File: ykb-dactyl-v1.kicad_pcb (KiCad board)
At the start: 2 copper layers, 55.7 x 57.2 mm, 68 parts, among them IC1 TXU0101DCKR, J1 JST_SH_BM10B-SRSS-TB_1x10-1MP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, J10 Conn_01x05, J11 Conn_01x02_MountingPin, J2 JST_SH_BM10B-SRSS-TB_1x10-1MP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, J3 JST_SH_BM10B-SRSS-TB_1x10-1MP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, J4 JST_SH_BM10B-SRSS-TB_1x10-1MP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, J5 JST_SH_BM10B-SRSS-TB_1x10-1MP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, J6 JST_SH_BM10B-SRSS-TB_1x10-1MP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, J7 JST_SH_BM12B-SRSS-TB_1x12-1MP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

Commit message: Add first version to the silkscreen
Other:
- board text added: "DV1_MB_REV_1.0"
- board text added: "Developer Preview 1"
- board text added: "YarmanKB"

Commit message: Update
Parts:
- added R7: 100K, Resistor_SMD:R_0402_1005Metric, F.Cu at (186.2, 112.8)
- added R8: 200K, Resistor_SMD:R_0402_1005Metric, F.Cu at (185.0, 112.8)
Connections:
- U1 pad P1.3: unconnected-(U1B-P1.03-PadP1.3) -> CHARGER_EN
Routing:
- net CHARGER_EN: track 0.00 -> 19.8 mm, vias 0 -> 2
- net +5V_USB: track 50.3 -> 62.3 mm, vias 2 -> 4
- net BAT_STAT_1: track 75.5 -> 78.0 mm
- net MUX3_A2: track 46.5 -> 48.5 mm
- net GND: track 39.6 -> 41.0 mm, vias 21 -> 42
- net MUX3_A1: track 47.5 -> 48.7 mm
- net MUX4_D: track 58.7 -> 59.7 mm
- net MUX3_A0: track 42.5 -> 43.4 mm
- net /MCU/RESET: track 57.8 -> 58.6 mm
- net /MCU/DBG_UART_NETCORE_RX: track 38.4 -> 39.0 mm

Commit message: Developer Preview 1
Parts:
- moved R4 0.90 mm to (175.0, 67.8)
- moved R5 0.90 mm to (175.0, 69.0)
- moved R6 0.90 mm to (175.0, 66.6)
- moved R71 0.20 mm to (179.5, 105.3)
- moved R72 0.20 mm to (179.5, 106.4)
- moved R73 0.20 mm to (179.5, 104.2)
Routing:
- net /MUXes/MUX1_S2: track 16.9 -> 22.1 mm
- net /MUXes/MUX1_S3: track 18.0 -> 22.8 mm
- net USB_DN_P: track 45.5 -> 41.5 mm
- net /MUXes/MUX2_S6: track 15.5 -> 19.4 mm
- net /MUXes/MUX2_S7: track 17.4 -> 21.3 mm
- net MUX1_D: track 36.2 -> 40.1 mm
- net ALARMB: track 7.70 -> 11.6 mm
- net /MUXes/MUX1_S5: track 17.2 -> 20.9 mm
- net /MUXes/MUX4_S3: track 20.5 -> 24.1 mm
- net /MUXes/MUX1_S6: track 16.2 -> 19.7 mm
- net /MUXes/MUX4_S5: track 15.2 -> 18.7 mm
- net /MUXes/MUX3_S1: track 14.6 -> 18.0 mm
- net MUX4_D: track 59.7 -> 63.0 mm
- net SW_P: track 55.2 -> 51.9 mm
- net /MUXes/MUX1_S8: track 15.9 -> 19.2 mm
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
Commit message: Developer Preview 2
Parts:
- removed D3: RB751S40,115, footprints:RB751S40115
- removed R4, R5, R6: 10K, Resistor_SMD:R_0402_1005Metric
- removed R7: 100K, Resistor_SMD:R_0402_1005Metric
- removed R8: 200K, Resistor_SMD:R_0402_1005Metric
- added Q21: BC847W, Package_TO_SOT_SMD:SOT-323_SC-70, F.Cu at (192.4, 76.1)
- added Q91: BC847BDW1, Package_TO_SOT_SMD:SOT-363_SC-70-6, F.Cu at (172.3, 73.3)
- added Q92: BC847W, Package_TO_SOT_SMD:SOT-323_SC-70, F.Cu at (186.2, 112.4)
- added R24: 100K, Resistor_SMD:R_0402_1005Metric, F.Cu at (189.8, 73.9)
- added R91: 100K, Resistor_SMD:R_0402_1005Metric, F.Cu at (188.2, 110.7)
- added R92: 47K, Resistor_SMD:R_0402_1005Metric, F.Cu at (178.0, 111.2)
- added R93: 100K, Resistor_SMD:R_0402_1005Metric, F.Cu at (174.9, 67.8)
- added R94: 47K, Resistor_SMD:R_0402_1005Metric, F.Cu at (174.3, 75.5)
- added R95: 100K, Resistor_SMD:R_0402_1005Metric, F.Cu at (174.9, 69.0)
- added R96: 47K, Resistor_SMD:R_0402_1005Metric, F.Cu at (172.9, 76.3)
- C52: value 1uF -> 22uF
- L31: footprint Inductor_SMD:L_0402_1005Metric -> Inductor_SMD:L_1008_2520Metric
- L41: footprint Inductor_SMD:L_0402_1005Metric -> Inductor_SMD:L_Murata_DFE201610P
- R51: value 1K -> 620
- R52: value 5K -> 18K
- R97: renamed from R1; value 600 -> 10K
- R98: renamed from R2; value 600 -> 10K
- R99: renamed from R3; value 600 -> 5K
- U2: footprint footprints:SON40P150X150X50-9N -> footprints:USP-8B06
- U7: value LC709203FXE-03MH -> MAX17048G+T10; footprint footprints:WLCSP9_1P60X1P76_ONS -> footprints:21-0168E_T822-3_MXM
- moved R73 3.18 mm to (182.6, 103.5), turned to -90 degrees
- moved R72 2.57 mm to (178.9, 103.9)
- moved C42 1.70 mm to (198.6, 109.7)
- moved R71 1.12 mm to (179.0, 106.3)
- moved C71 1.04 mm to (180.3, 108.8)
- moved U7 0.93 mm to (182.2, 106.2), turned to 90 degrees
- moved L41 0.92 mm to (196.7, 109.9)
- moved R23 0.91 mm to (190.9, 73.9)
- moved L31 0.74 mm to (192.5, 104.3)
- moved R43 0.40 mm to (199.3, 112.1)
- moved R44 0.40 mm to (197.1, 112.1)
- moved U2 0.35 mm to (186.2, 73.2), turned to 90 degrees
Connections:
- net /MCU/DBG_LED_P renamed /MCU/DBG_LED_LED
- D1 pad 3: +3.3V_SYS -> VCC_PRESYS
- D1 pad 4: /MCU/BAT_STAT_1_P -> /MCU/BAT_STAT_1_LED
- D1 pad 5: +3.3V_SYS -> VCC_PRESYS
- D1 pad 6: /MCU/BAT_STAT_2_P -> /MCU/BAT_STAT_2_LED
- D2 pad 3: +3.3V_SYS -> VCC_PRESYS
- D2 pad 4: /MCU/BAT_STAT_1_P -> /MCU/BAT_STAT_1_LED
- D2 pad 5: +3.3V_SYS -> VCC_PRESYS
- D2 pad 6: /MCU/BAT_STAT_2_P -> /MCU/BAT_STAT_2_LED
- R71 pad 1: SDA -> SCL
- R72 pad 1: SCL -> SDA
- R73 pad 1: ALARMB -> GND
- R73 pad 2: +3.3V_SYS -> Net-(U7-QSTRT)
- R97 pad 2: /MCU/BAT_STAT_1_P -> /MCU/BAT_STAT_1_LED
- R98 pad 2: /MCU/BAT_STAT_2_P -> /MCU/BAT_STAT_2_LED
- U1 pad P0.17: BAT_STAT_1 -> /MCU/BAT_STAT_1_P
- U1 pad P0.18: BAT_STAT_2 -> /MCU/BAT_STAT_2_P
- U1 pad P1.2: ALARMB -> unconnected-(U1B-P1.02-PadP1.2)
- U1 pad P1.3: CHARGER_EN -> /MCU/CHARGER_EN
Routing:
- net VCC_PRESYS: track 37.6 -> 88.7 mm, vias 2 -> 8
- net /MCU/BAT_STAT_2_LED: track 0.00 -> 33.4 mm, vias 0 -> 2
- net /MCU/BAT_STAT_1_LED: track 0.00 -> 31.6 mm, vias 0 -> 2
- net /MCU/CHARGER_EN: track 0.00 -> 21.0 mm, vias 0 -> 2
- net CHARGER_EN: track 19.8 -> 0.00 mm, vias 2 -> 0
- net ALARMB: track 11.6 -> 0.00 mm, vias 2 -> 0
- net Net-(Q21-B): track 0.00 -> 11.4 mm, vias 0 -> 2
- net Net-(Q91A-B1): track 0.00 -> 10.7 mm, vias 0 -> 2
- net /MCU/BAT_STAT_1_P: track 29.3 -> 39.2 mm
- net GND: track 41.0 -> 32.8 mm, vias 50 -> 60
- net Net-(Q91B-B2): track 0.00 -> 5.57 mm
- net +3.3V_SYS: track 245.2 -> 240.1 mm
- net +5V_USB: track 62.4 -> 57.8 mm
- net +5V_SYS: track 110.5 -> 114.5 mm
- net SCL: track 15.4 -> 12.3 mm
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
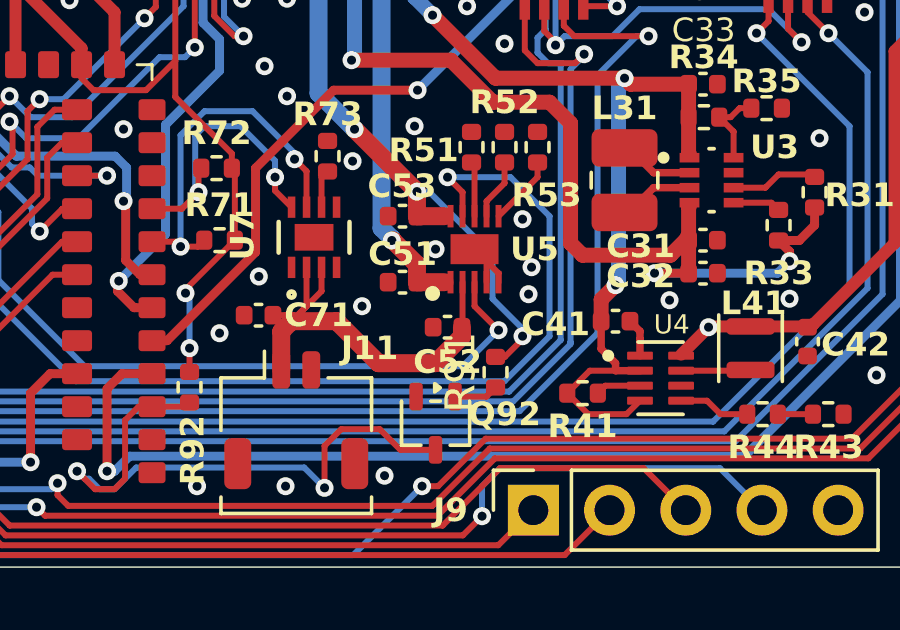
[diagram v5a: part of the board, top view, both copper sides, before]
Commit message: Fix silkscreen for Developer Preview 2
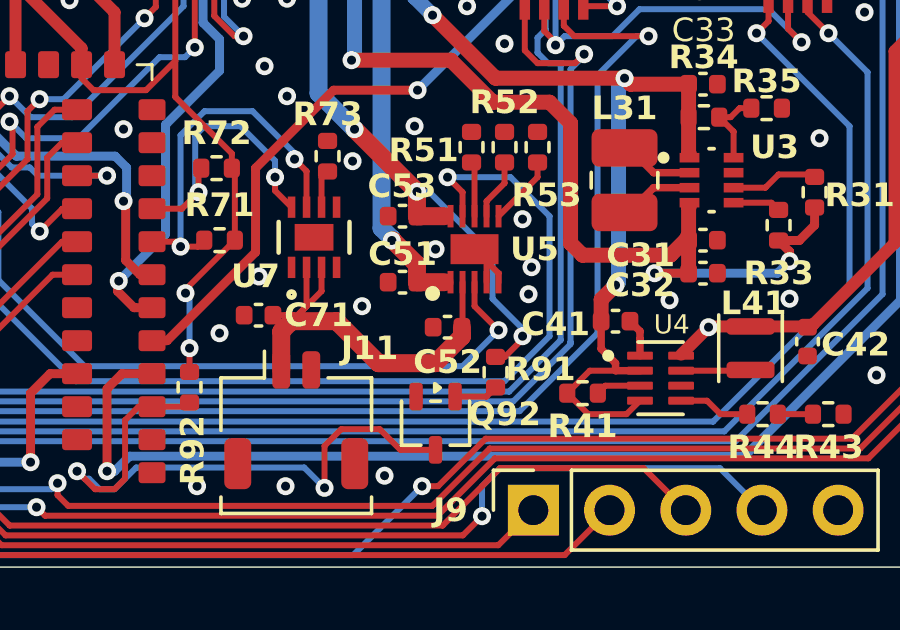
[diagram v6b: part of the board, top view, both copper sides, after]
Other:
- board text added: "Developer Preview 2"
- board text removed: "Developer Preview 1"
